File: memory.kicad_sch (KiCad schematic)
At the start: 43 parts, among them Q5 DMG1012T-7, Q7 DMG1012T-7, Q8 DMG1012T-7, U10 TPS2117DRLR, U2 SDINBDG4-8G, U3 MT25QL01GBBB1EW9-0SIT, U9 TPS2117DRLR

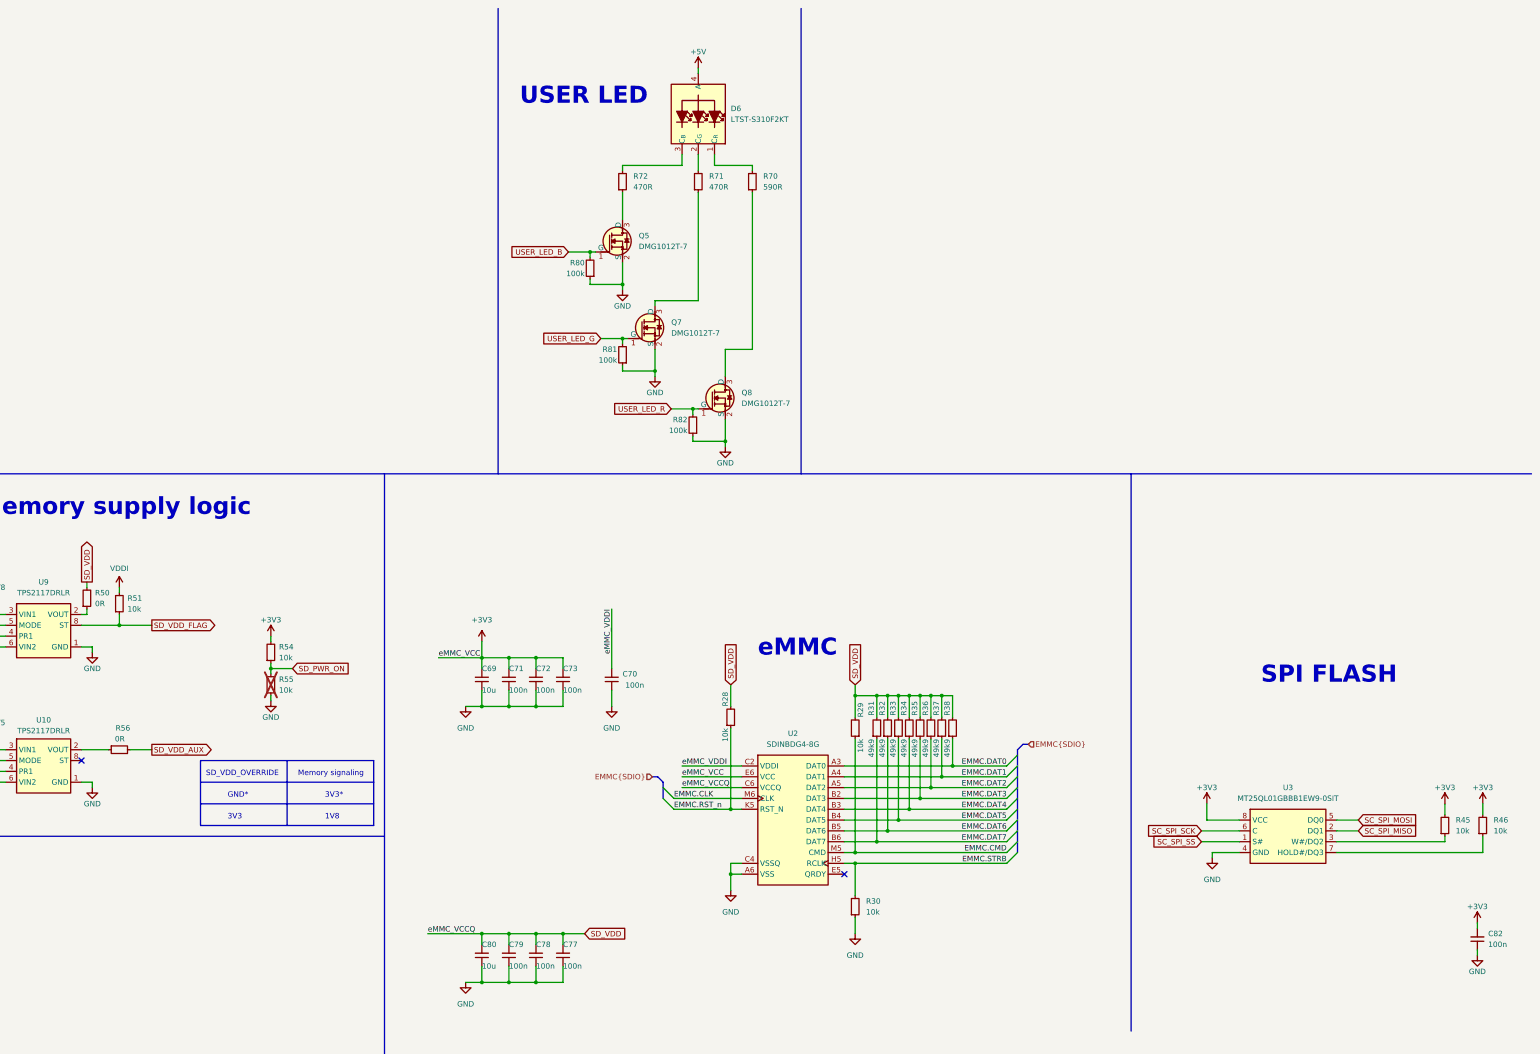
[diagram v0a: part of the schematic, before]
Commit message: [#57505] Continue migration to hierarchical schematic
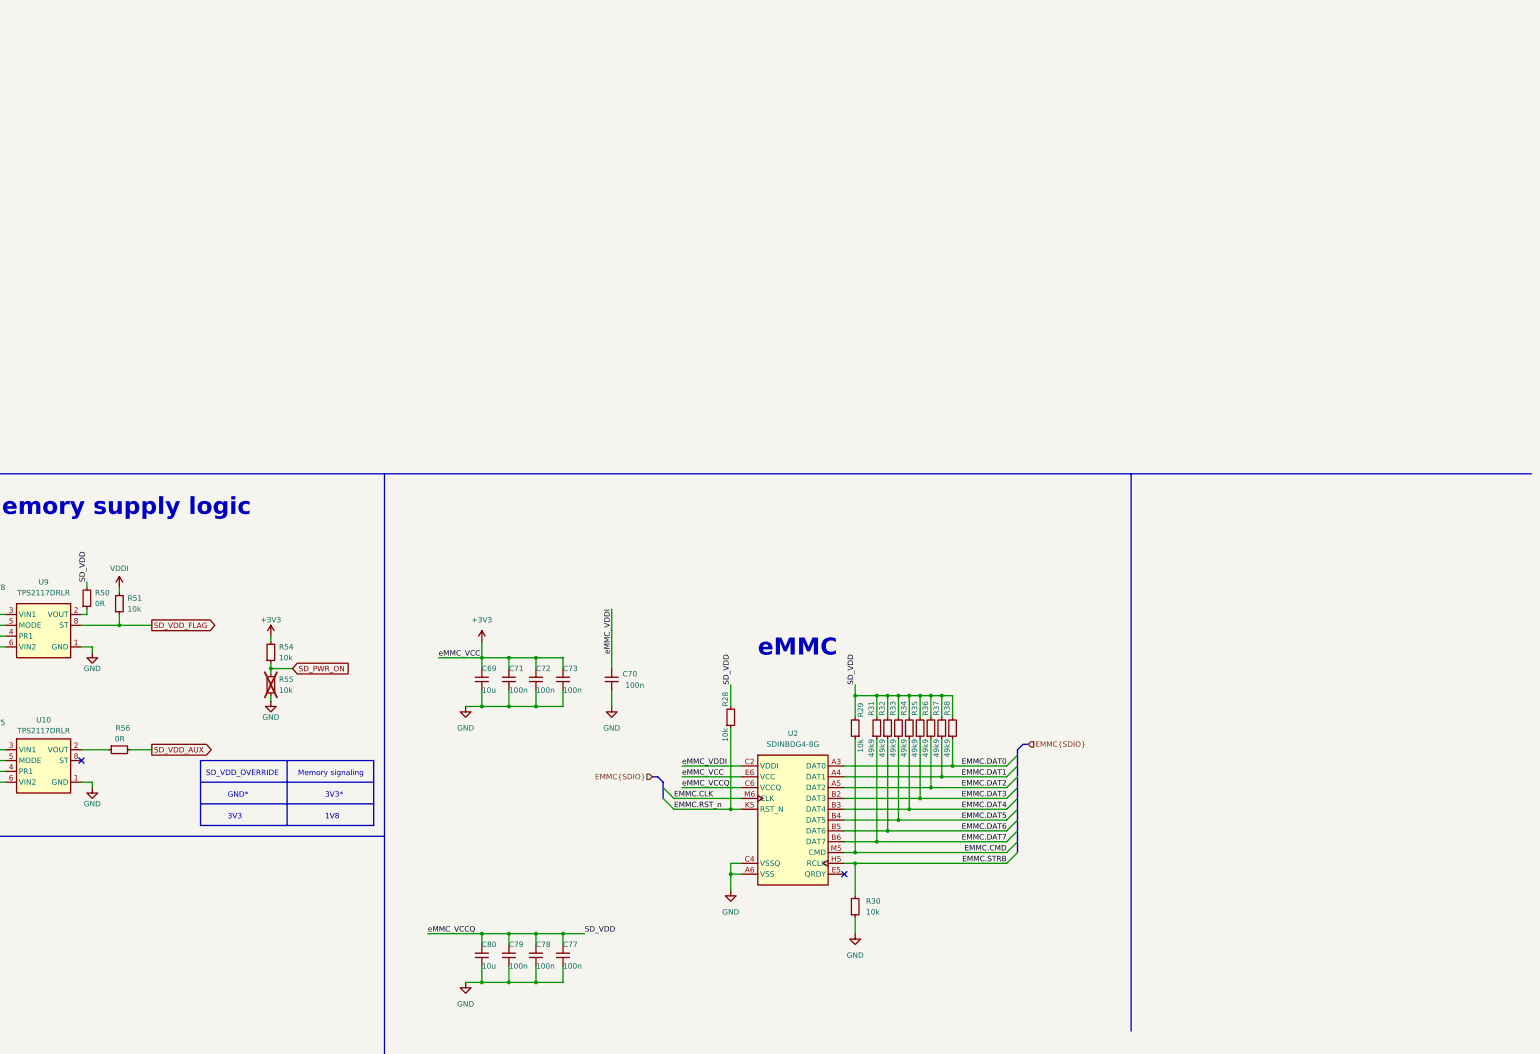
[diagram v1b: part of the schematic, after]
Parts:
- removed C82: C_100n_0402, antmicro-footprints:C_0402_1005Metric, symbol antmicroCapacitors0402:C_100n_0402
- removed D6: LED_RGB_1204_LTST-S310F2KT_Horizontal, antmicro-footprints:LED_1204_3210Metric_RGB, symbol antmicroLEDIndicationDiscrete:LED_RGB_1204_LTST-S310F2KT_Horizontal
- removed Q5, Q7, Q8: DMG1012T-7, antmicro-footprints:SOT-523, symbol antmicroTransistorsFETsMOSFETsSingle:DMG1012T-7
- removed R45, R46: R_10k_0402, antmicro-footprints:R_0402_1005Metric, symbol antmicroResistors0402:R_10k_0402
- removed R70: R_590R_0402, antmicro-footprints:R_0402_1005Metric, symbol antmicroResistors0402:R_590R_0402
- removed R71, R72: R_470R_0402, antmicro-footprints:R_0402_1005Metric, symbol antmicroResistors0402:R_470R_0402
- removed R80, R81, R82: R_100k_0402, antmicro-footprints:R_0402_1005Metric, symbol antmicroResistors0402:R_100k_0402
- removed U3: MT25QL01GBBB1EW9-0SIT, antmicro-footprints:W-PDFN-8-1EP_8x6mm_P1.27mm_EP4.3x3.4mm, symbol antmicroMemory:MT25QL01GBBB1EW9-0SIT
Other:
- note removed: "SPI FLASH"
- note removed: "USER LED"

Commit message: [#57505] Finish defining buses
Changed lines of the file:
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@@
   (junction (at 219.71 200.66) (diameter 0) (color 0 0 0 0)
   )
-  (junction (at 161.29 229.87) (diameter 0) (color 0 0 0 0)
-  )
   (junction (at 248.92 213.36) (diameter 0) (color 0 0 0 0)
   )
@@
     (stroke (width 0) (type default))
   )
-  (wire (pts (xy 151.13 165.1) (xy 161.29 165.1))
-    (stroke (width 0) (type default))
-  )
   (wire (pts (xy 67.31 162.56) (xy 69.85 162.56))
     (stroke (width 0) (type default))
@@
     (stroke (width 0) (type default))
   )
-  (wire (pts (xy 148.59 229.87) (xy 161.29 229.87))
-    (stroke (width 0) (type default))
-  )
   (bus (pts (xy 287.02 190.5) (xy 287.02 193.04))
     (stroke (width 0) (type default))
@@
     (stroke (width 0) (type default))
   )
-  (wire (pts (xy 208.28 193.04) (xy 222.25 193.04))
+  (wire (pts (xy 206.375 193.04) (xy 206.375 188.595))
+    (stroke (width 0) (type default))
+  )
+  (wire (pts (xy 206.375 193.04) (xy 222.25 193.04))
     (stroke (width 0) (type default))
   )
@@
     (stroke (width 0) (type default))
   )
+  (wire (pts (xy 123.825 85.09) (xy 114.3 85.09))
+    (stroke (width 0) (type default))
+  )
   (wire (pts (xy 180.34 172.72) (xy 180.34 176.53))
     (stroke (width 0) (type default))
@@
     (effects (font (size 1.27 1.27)) (justify right bottom))
   )
+  (label "SD_VDD" (at 208.28 195.58 0) (fields_autoplaced)
+    (effects (font (size 1.27 1.27)) (justify left bottom))
+  )
   (label "EMMC.RST_n" (at 206.375 200.66 0) (fields_autoplaced)
     (effects (font (size 1.27 1.27)) (justify left bottom))
@@
     (effects (font (size 1.27 1.27)) (justify right bottom))
   )
-  (label "eMMC_VCCQ" (at 208.28 195.58 0) (fields_autoplaced)
-    (effects (font (size 1.27 1.27)) (justify left bottom))
-  )
   (label "EMMC.DAT4" (at 284.48 200.66 180) (fields_autoplaced)
     (effects (font (size 1.27 1.27)) (justify right bottom))
   )
-  (label "eMMC_VCC" (at 151.13 165.1 0) (fields_autoplaced)
-    (effects (font (size 1.27 1.27)) (justify left bottom))
+  (label "SD_VDD" (at 123.825 85.09 180) (fields_autoplaced)
+    (effects (font (size 1.27 1.27)) (justify right bottom))
   )
   (label "EMMC.DAT6" (at 284.48 205.74 180) (fields_autoplaced)
@@
     (effects (font (size 1.27 1.27)) (justify right bottom))
   )
-  (label "eMMC_VCCQ" (at 148.59 229.87 0) (fields_autoplaced)
-    (effects (font (size 1.27 1.27)) (justify left bottom))
-  )
   (label "EMMC.CMD" (at 284.48 210.82 180) (fields_autoplaced)
     (effects (font (size 1.27 1.27)) (justify right bottom))
   )
-  (label "eMMC_VCC" (at 208.28 193.04 0) (fields_autoplaced)
-    (effects (font (size 1.27 1.27)) (justify left bottom))
-  )
   (label "EMMC.DAT2" (at 284.48 195.58 180) (fields_autoplaced)
     (effects (font (size 1.27 1.27)) (justify right bottom))
@@
     )
   )
+  (global_label "SD_VDD" (shape input) (at 114.3 85.09 180) (fields_autoplaced)
+    (effects (font (size 1.27 1.27)) (justify right))
+    (property "Intersheetrefs" "${INTERSHEET_REFS}" (at 104.2391 85.09 0)
+      (effects (font (size 1.27 1.27)) (justify right))
+    )
+  )
   (hierarchical_label "EMMC{SDIO}" (shape input) (at 201.295 193.04 180) (fields_autoplaced)
     (effects (font (size 1.27 1.27)) (justify right))
@@
         )
       )
+    )
+  )
+  (symbol (lib_id "antmicropower:+3V3") (at 206.375 188.595 0) (unit 1)
+    (in_bom yes) (on_board yes) (dnp no) (fields_autoplaced)
+    (property "Reference" "#PWR0358" (at 221.615 191.135 0)
+      (effects (font (size 1.27 1.27) (thickness 0.15)) (justify left bottom) hide)
+    )
+    (property "Value" "+3V3" (at 206.375 183.515 0)
+      (effects (font (size 1.27 1.27) (thickness 0.15)))
+    )
+    (property "Footprint" "" (at 221.615 196.215 0)
+      (effects (font (size 1.27 1.27) (thickness 0.15)) (justify left bottom) hide)
+    )
+    (property "Datasheet" "" (at 221.615 198.755 0)
+      (effects (font (size 1.27 1.27) (thickness 0.15)) (justify left bottom) hide)
+    )
+    (property "Author" "Antmicro" (at 221.615 196.215 0)
+      (effects (font (size 1.27 1.27) (thickness 0.15)) (justify left bottom) hide)
+    )
+    (property "License" "Apache-2.0" (at 221.615 198.755 0)
+      (effects (font (size 1.27 1.27) (thickness 0.15)) (justify left bottom) hide)
+    )
+    (pin "1")
+    (instances
+      (project "polarfire-som"
+        (path "/db4a0d3e-2eb3-499e-977d-6eb378cfd3ed/6b5c9386-08fc-46bf-a582-c320c1d104da"
+          (reference "#PWR0358") (unit 1)
+        )
+      )

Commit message: [#57422] Finishing touches
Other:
- moved on the sheet: C69, C70, C71, C72, C73, C77, C78, C79, C80, R28, R29, R30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

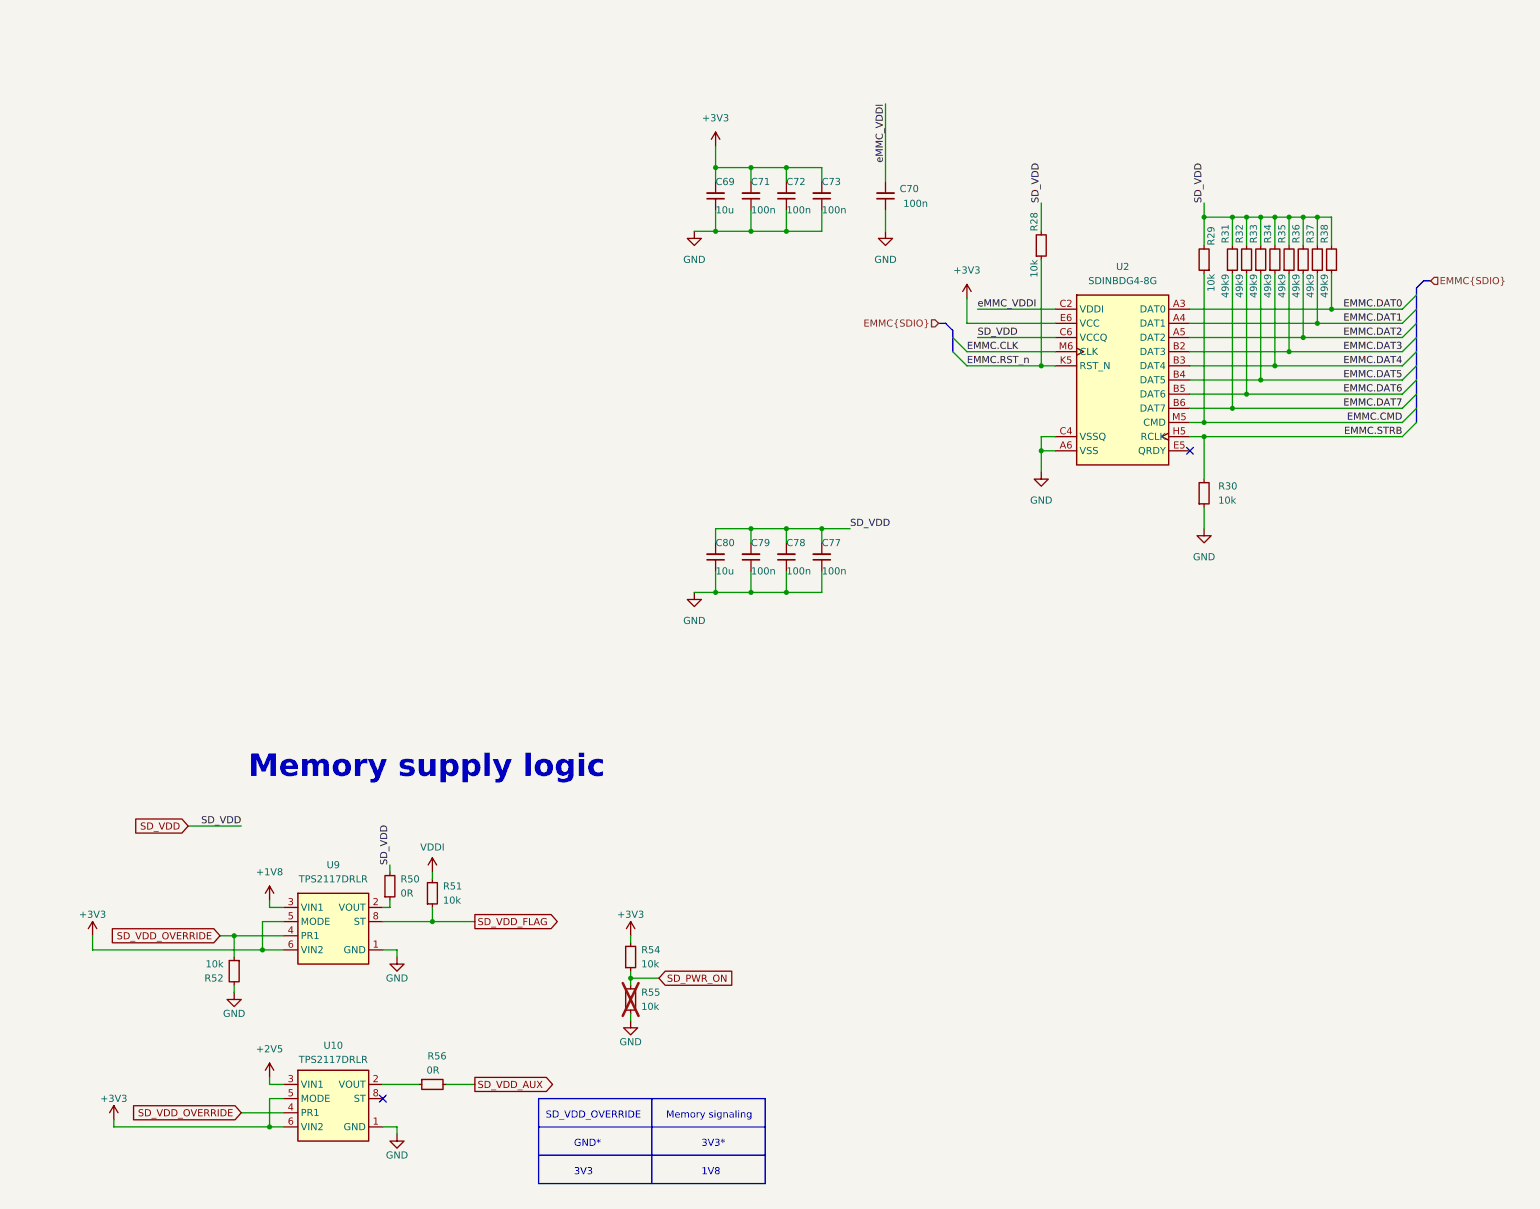
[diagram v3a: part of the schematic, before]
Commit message: [#57422] Align schematics
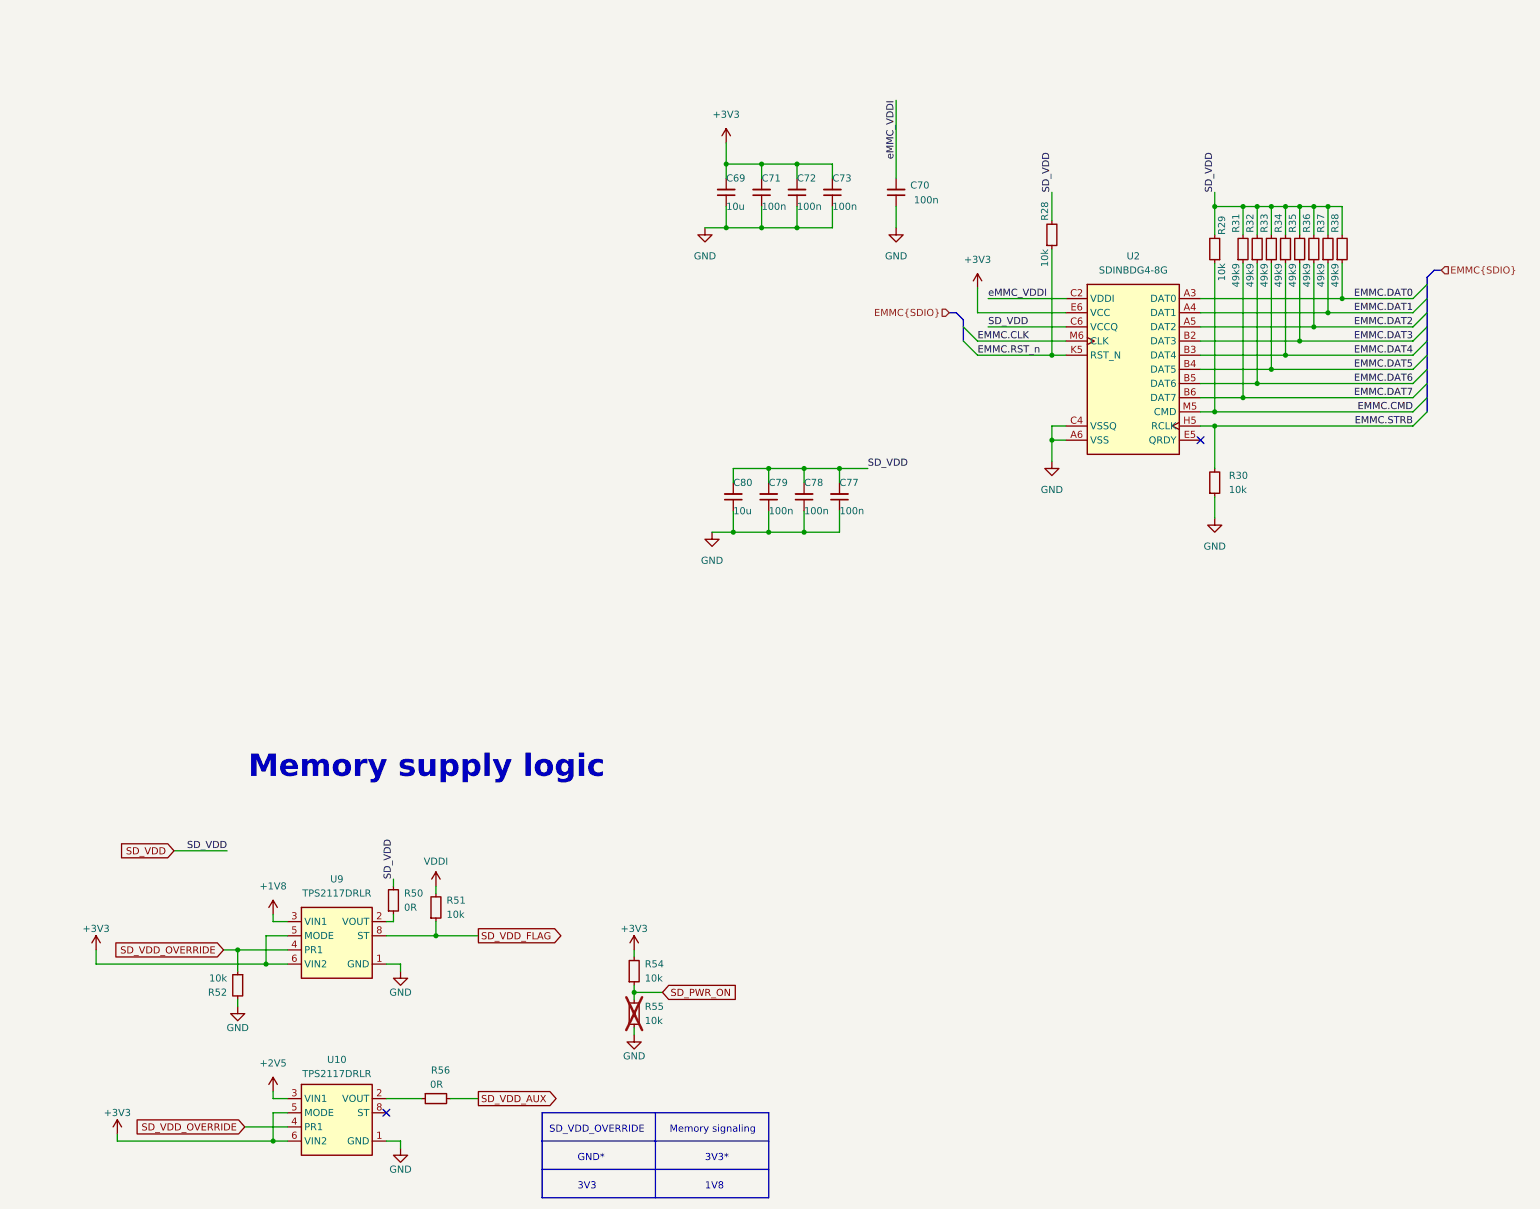
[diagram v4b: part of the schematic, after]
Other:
- moved on the sheet: C69, C70, C71, C72, C73, C77, C78, C79, C80, R28, R29, R30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
